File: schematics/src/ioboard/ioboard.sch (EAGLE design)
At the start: 70 parts, among them IC1 TL072P, IC2 TL072P, IC3 TL072P, T1 2N3904, T2 2N3904

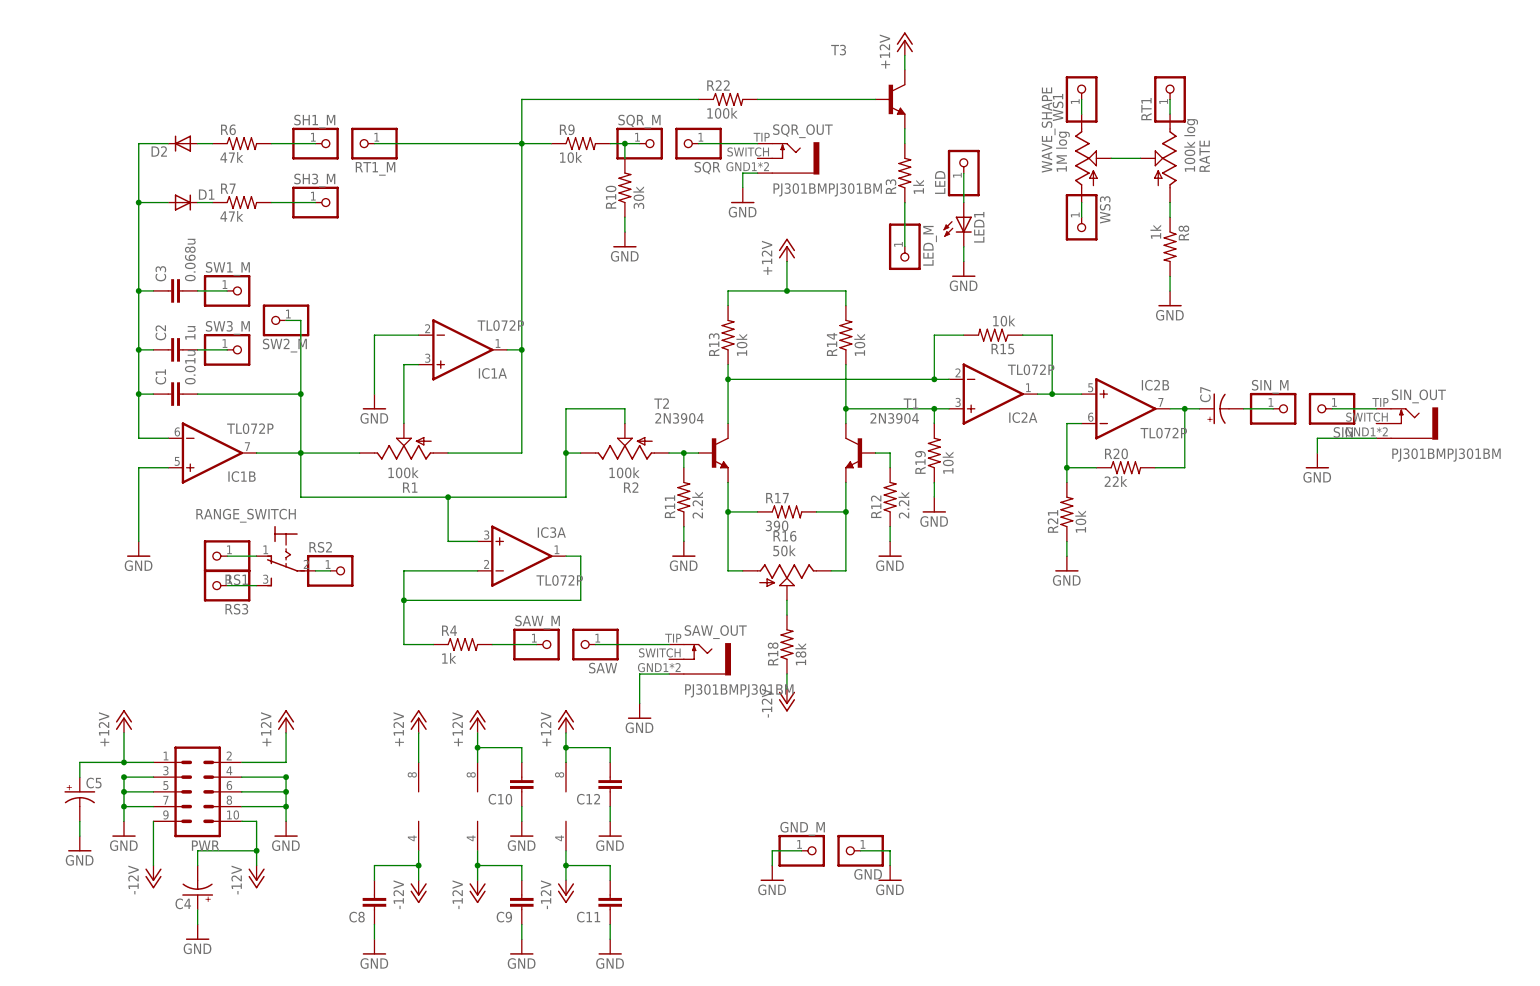
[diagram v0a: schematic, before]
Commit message: Updated schematics with missing values
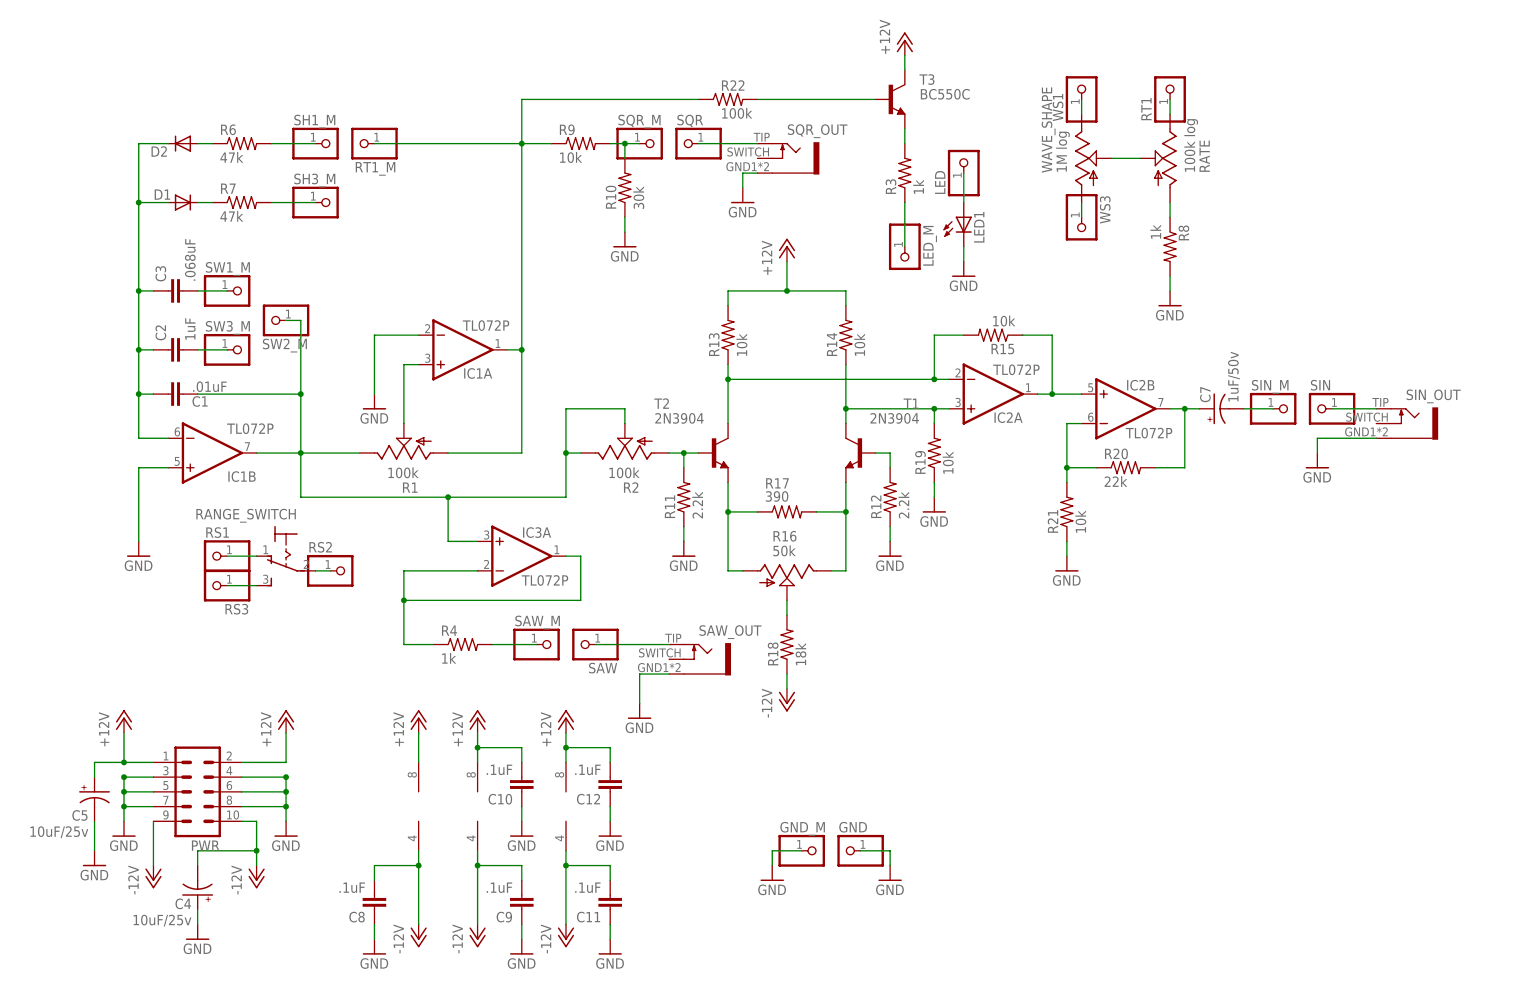
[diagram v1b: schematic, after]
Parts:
- C1: value 0.01u -> .01uF
- C10, C11, C12, C8, C9: value (none) -> .1uF
- C2: value 1u -> 1uF
- C3: value 0.068u -> .068uF
- C4, C5: value (none) -> 10uF/25v
- C7: value (none) -> 1uF/50v
- T3: value (none) -> BC550C
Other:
- moved on the sheet: C5
